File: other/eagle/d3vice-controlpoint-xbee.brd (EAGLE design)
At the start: 56.8 x 52.1 mm, 15 parts, among them IC3 74LS125N

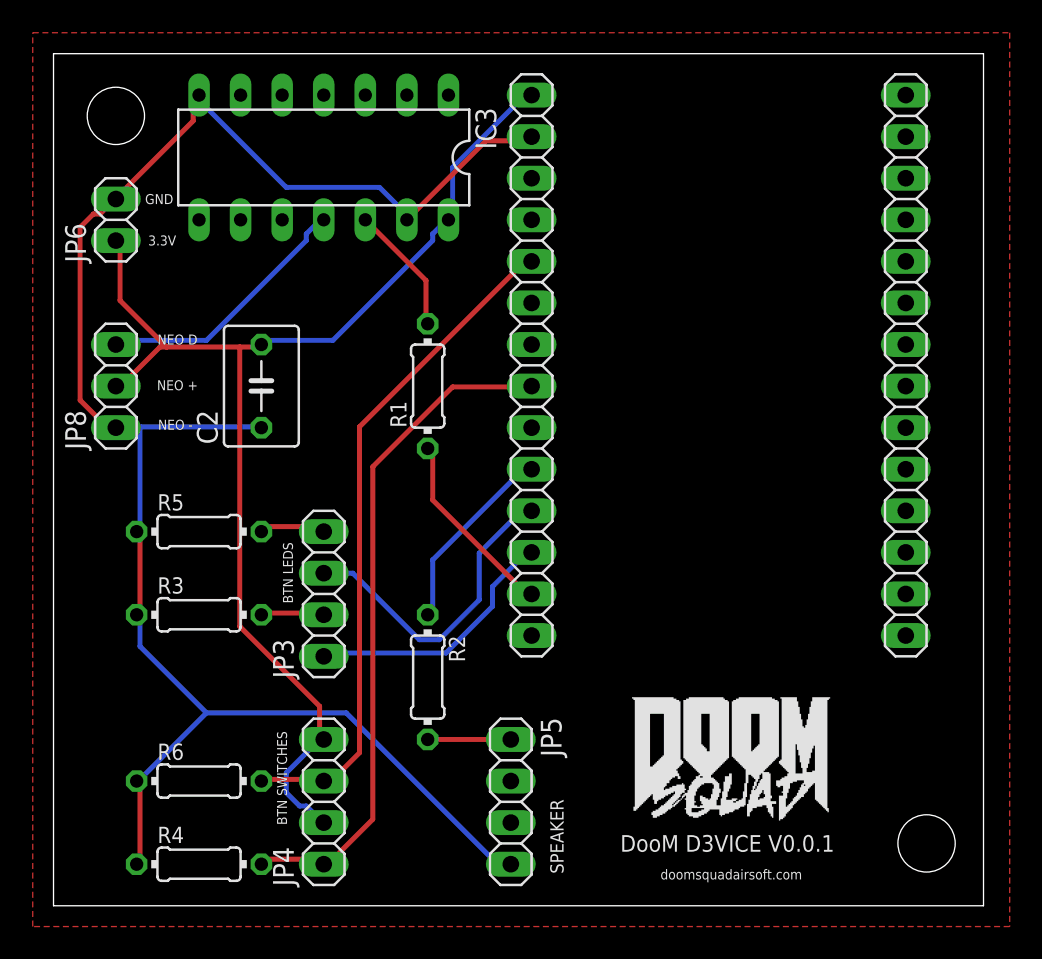
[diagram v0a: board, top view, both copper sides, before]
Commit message: added battery voltage circuit
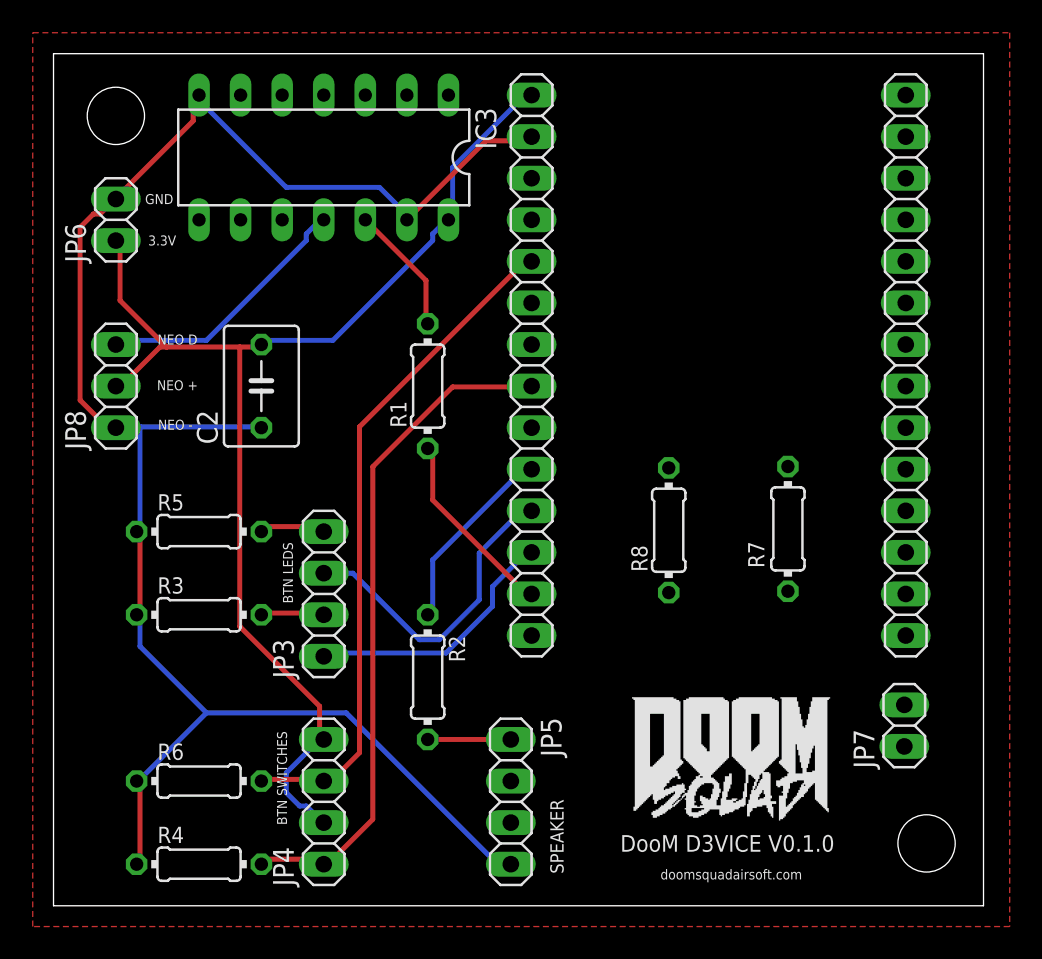
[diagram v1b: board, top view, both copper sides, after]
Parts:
- added JP7: (no value), pinhead:1X02
- added R7: 10K, eagle-ltspice:0204/7
- added R8: 100K, eagle-ltspice:0204/7
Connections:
- new net 0: JP7.2, R7.2
- new net N$1: JP2.11, R7.1, R8.2
- new net N$12: JP7.1, R8.1
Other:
- board text added: "DooM D3VICE V0.1.0"
- board text removed: "DooM D3VICE V0.0.1"
